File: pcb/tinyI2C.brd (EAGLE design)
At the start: 105.6 x 84.4 mm, 39 parts, among them IC1 74LVC1G125DCK, IC2 74LVC1G125DCK, IC3 IC_LDO_MIC5355, Q1 12MHz, U1 LPC824M201JHI33, X1 TSW-112-02-S-S, X2 TSW-112-02-S-S, X3 TSW-106-02-S-S-RA, X4 TSW-102-02-S-S, X5 TSW-102-02-S-S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

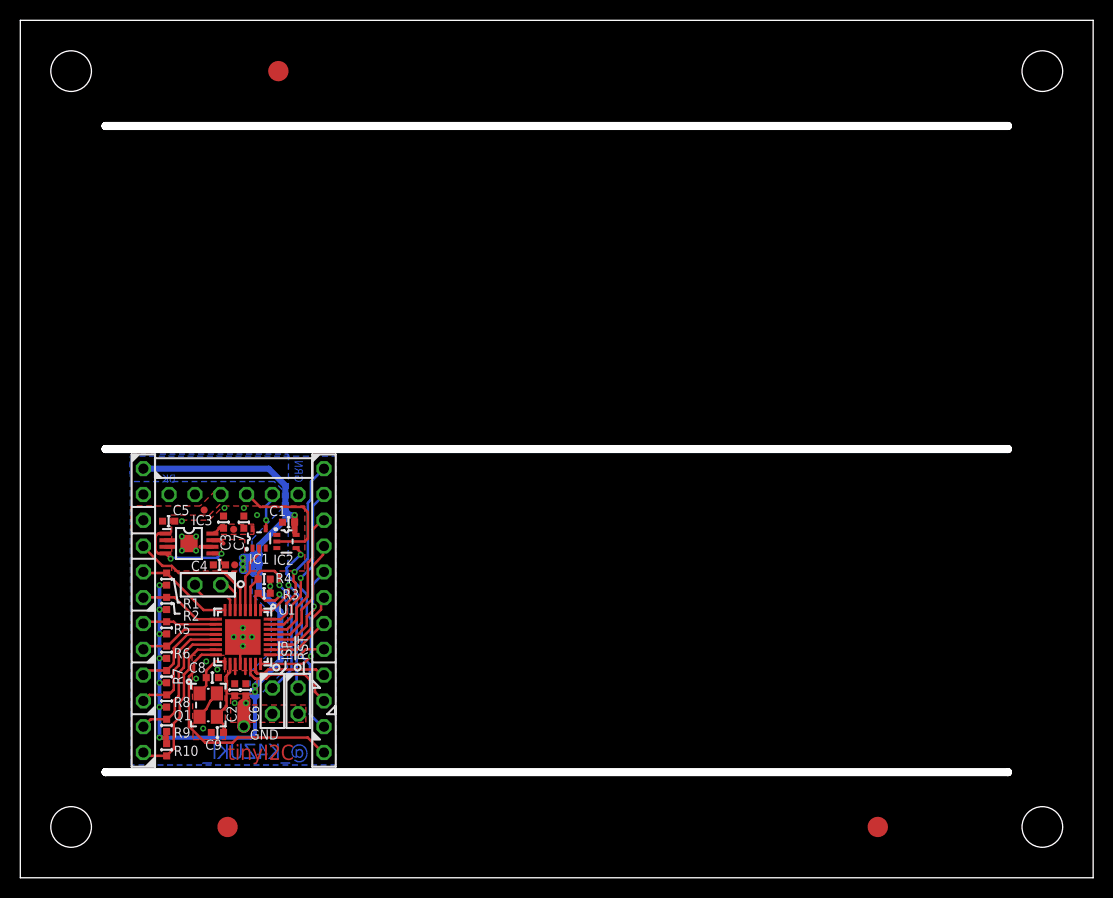
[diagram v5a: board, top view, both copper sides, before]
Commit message: [ PCB ] outline size shrinked
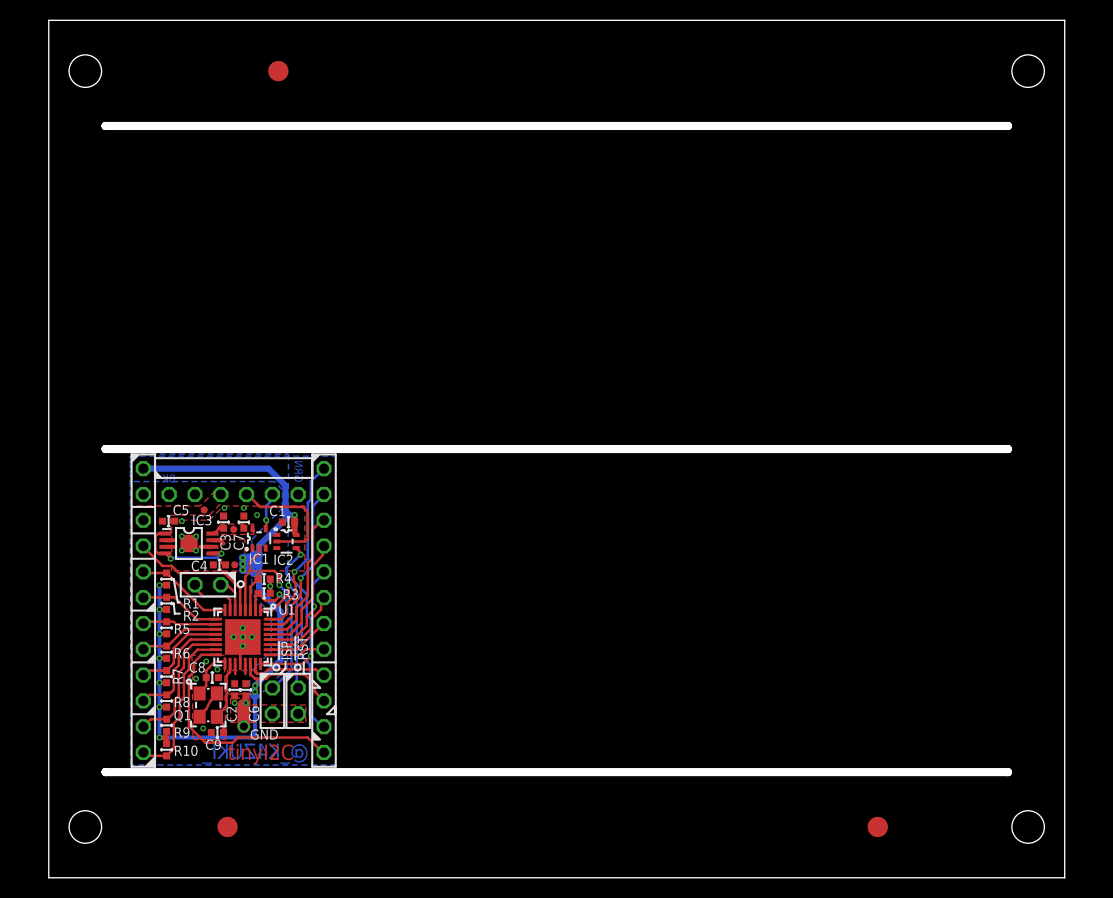
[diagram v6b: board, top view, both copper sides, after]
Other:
- board size 105.6 x 84.4 mm -> 100 x 84.4 mm
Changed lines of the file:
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@@
 <layer number="98" name="Guide" color="6" fill="1" visible="no" active="no"/>
 <layer number="100" name="NonViaHole" color="7" fill="1" visible="no" active="yes"/>
-<layer number="101" name="PlacementGuide" color="7" fill="1" visible="yes" active="yes"/>
+<layer number="101" name="PlacementGuide" color="7" fill="1" visible="no" active="yes"/>
 <layer number="102" name="Vscore" color="7" fill="1" visible="yes" active="yes"/>
 <layer number="103" name="not_populated" color="7" fill="1" visible="no" active="yes"/>
@@
 <wire x1="52.8" y1="84.5" x2="52.8" y2="0.1" width="0.8" layer="102"/>
 <wire x1="74" y1="84.4" x2="74" y2="0" width="0.8" layer="102"/>
-<hole x="5" y="79.4" drill="4"/>
-<hole x="100.6" y="5" drill="4"/>
-<hole x="100.6" y="79.4" drill="4"/>
-<hole x="5" y="5" drill="4"/>
-<wire x1="0" y1="84.4" x2="105.6" y2="84.4" width="0" layer="20"/>
-<wire x1="0" y1="0" x2="105.6" y2="0" width="0" layer="20"/>
-<dimension x1="0" y1="0" x2="105.6" y2="0" x3="52.8" y3="-9" textsize="1.27" textratio="10" layer="47" visible="yes"/>
+<hole x="6.4" y="79.4" drill="3.2"/>
+<hole x="99.2" y="5" drill="3.2"/>
+<hole x="99.2" y="79.4" drill="3.2"/>
+<hole x="6.4" y="5" drill="3.2"/>
+<wire x1="2.8" y1="84.4" x2="102.8" y2="84.4" width="0" layer="20"/>
+<wire x1="2.8" y1="0" x2="102.8" y2="0" width="0" layer="20"/>
+<dimension x1="2.8" y1="0" x2="102.8" y2="0" x3="52.8" y3="-9" textsize="1.27" textratio="10" layer="47" visible="yes"/>
 <dimension x1="10.8" y1="0" x2="31.2" y2="0" x3="21" y3="-4" textsize="1.27" textratio="10" layer="47" visible="yes"/>
-<dimension x1="0" y1="0" x2="0" y2="84.4" x3="-16" y3="42.2" textsize="1.27" textratio="10" layer="47" visible="yes"/>
-<dimension x1="0" y1="10" x2="0" y2="0" x3="-13" y3="5" textsize="1.27" textratio="10" layer="47" visible="yes"/>
-<dimension x1="0" y1="10.8" x2="0" y2="41.8" x3="-13" y3="26.3" textsize="1.27" textratio="10" layer="47" visible="yes"/>
-<dimension x1="0" y1="42.6" x2="0" y2="73.6" x3="-13" y3="58.1" textsize="1.27" textratio="10" layer="47" visible="yes"/>
-<dimension x1="0" y1="84.4" x2="0" y2="74.4" x3="-13" y3="79.4" textsize="1.27" textratio="10" layer="47" visible="yes"/>
+<dimension x1="2.8" y1="0" x2="2.8" y2="84.4" x3="-13.2" y3="42.2" textsize="1.27" textratio="10" layer="47" visible="yes"/>
+<dimension x1="2.8" y1="10" x2="2.8" y2="0" x3="-10.2" y3="5" textsize="1.27" textratio="10" layer="47" visible="yes"/>
+<dimension x1="2.8" y1="10.8" x2="2.8" y2="41.8" x3="-10.2" y3="26.3" textsize="1.27" textratio="10" layer="47" visible="yes"/>
+<dimension x1="2.8" y1="42.6" x2="2.8" y2="73.6" x3="-10.2" y3="58.1" textsize="1.27" textratio="10" layer="47" visible="yes"/>
+<dimension x1="2.8" y1="84.4" x2="2.8" y2="74.4" x3="-10.2" y3="79.4" textsize="1.27" textratio="10" layer="47" visible="yes"/>
 <dimension x1="12.11" y1="26.3" x2="29.89" y2="26.3" x3="21" y3="1.5" textsize="1.27" textratio="10" layer="47" precision="5" visible="yes"/>
 <dimension x1="32" y1="0" x2="52.4" y2="0" x3="42.2" y3="-4" textsize="1.27" textratio="10" layer="47" visible="yes"/>
@@
 <rectangle x1="23.4" y1="79.4" x2="25.4" y2="81.4" layer="29"/>
 <rectangle x1="82.4" y1="5" x2="84.4" y2="7" layer="29"/>
-<wire x1="73.7" y1="42" x2="74.1" y2="42" width="0" layer="24"/>
-<wire x1="74.1" y1="42" x2="74.1" y2="41.6" width="0" layer="24"/>
 <wire x1="11" y1="41.6" x2="30.9" y2="41.6" width="0.4" layer="42"/>
 <wire x1="11" y1="11" x2="11" y2="41.6" width="0.4" layer="42"/>
@@
 <wire x1="22.4" y1="35.2" x2="21.6" y2="35.2" width="0.1" layer="41"/>
 <rectangle x1="18.4" y1="5" x2="20.4" y2="7" layer="29"/>
-<wire x1="0" y1="84.4" x2="0" y2="0" width="0" layer="20"/>
-<wire x1="105.6" y1="84.4" x2="105.6" y2="0" width="0" layer="20"/>
-<dimension x1="0" y1="0" x2="10" y2="0" x3="5" y3="-4" textsize="1.27" textratio="10" layer="47" visible="yes"/>
-<dimension x1="95.6" y1="0" x2="105.6" y2="0" x3="100.6" y3="-4" textsize="1.27" textratio="10" layer="47" visible="yes"/>
+<wire x1="2.8" y1="84.4" x2="2.8" y2="0" width="0" layer="20"/>
+<wire x1="102.8" y1="84.4" x2="102.8" y2="0" width="0" layer="20"/>
+<dimension x1="2.8" y1="0" x2="10" y2="0" x3="6.4" y3="-4" textsize="1.27" textratio="10" layer="47" visible="yes"/>
+<dimension x1="95.6" y1="0" x2="102.8" y2="0" x3="99.2" y3="-4" textsize="1.27" textratio="10" layer="47" visible="yes"/>
 <polygon width="0.5" layer="46">
 <vertex x="8.4" y="74.15"/>
@@
 <rectangle x1="84.4" y1="3" x2="86.4" y2="5" layer="29"/>
 <rectangle x1="82.4" y1="3" x2="84.4" y2="5" layer="29"/>
+<dimension x1="53.2" y1="0" x2="73.6" y2="0" x3="63.4" y3="-4" textsize="1.27" textratio="10" layer="47" visible="yes"/>
 </plain>
 <attributes>
